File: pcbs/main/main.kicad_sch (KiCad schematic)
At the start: 15 parts

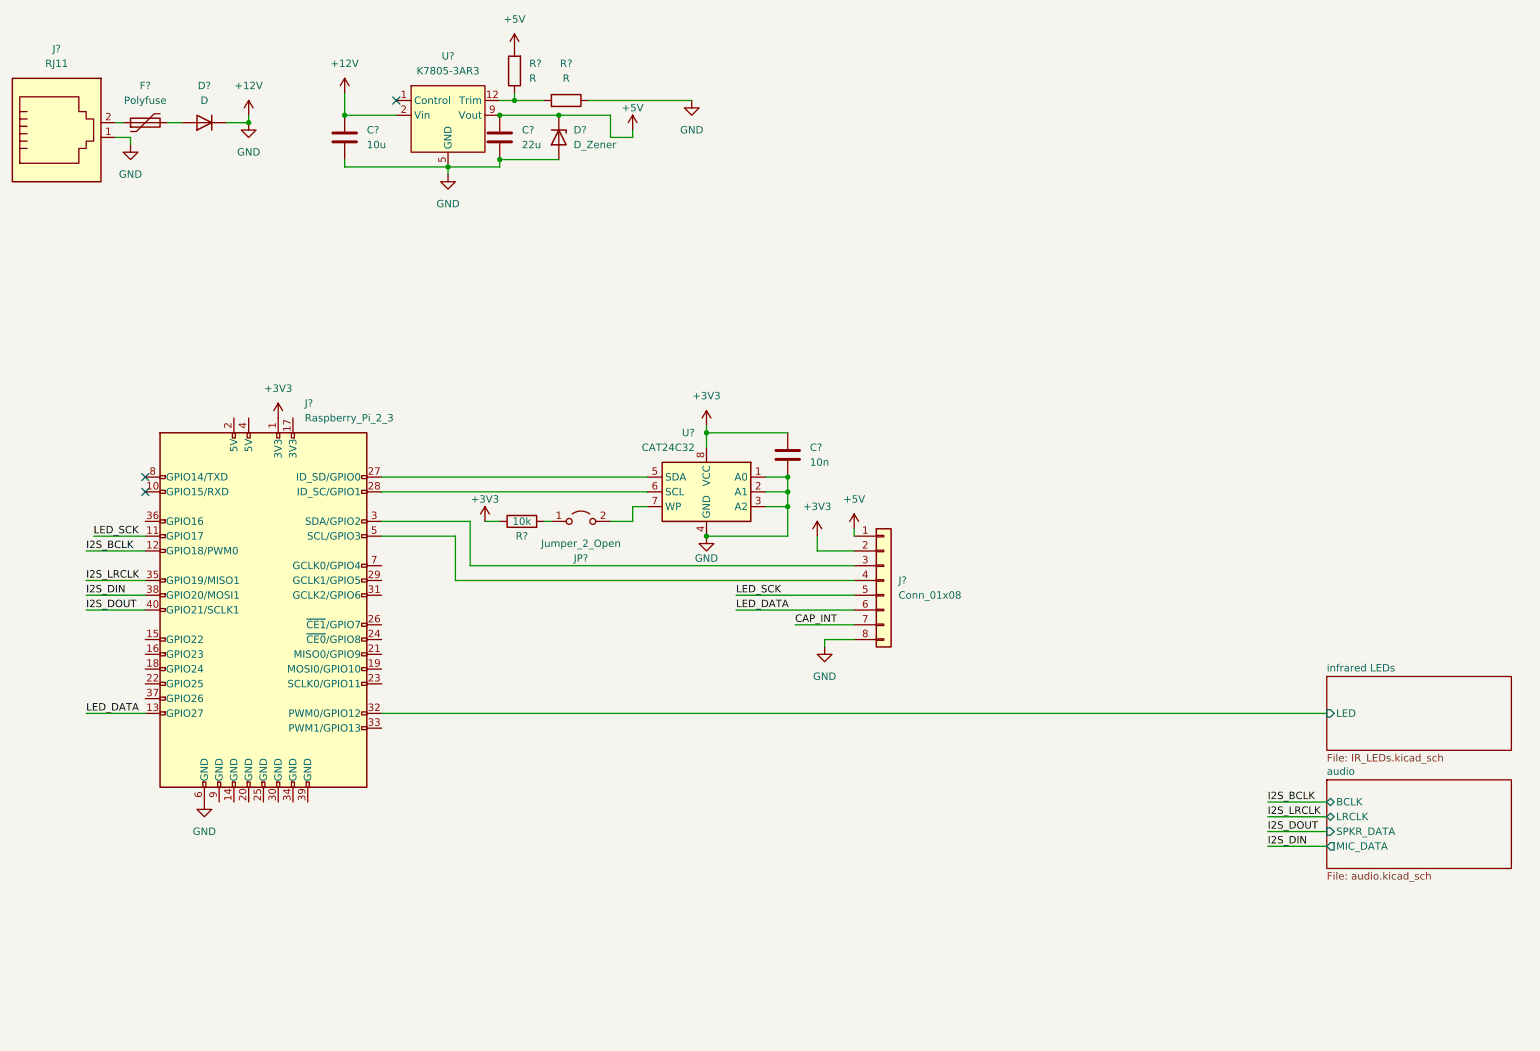
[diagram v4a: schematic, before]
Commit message: Add door release functionality
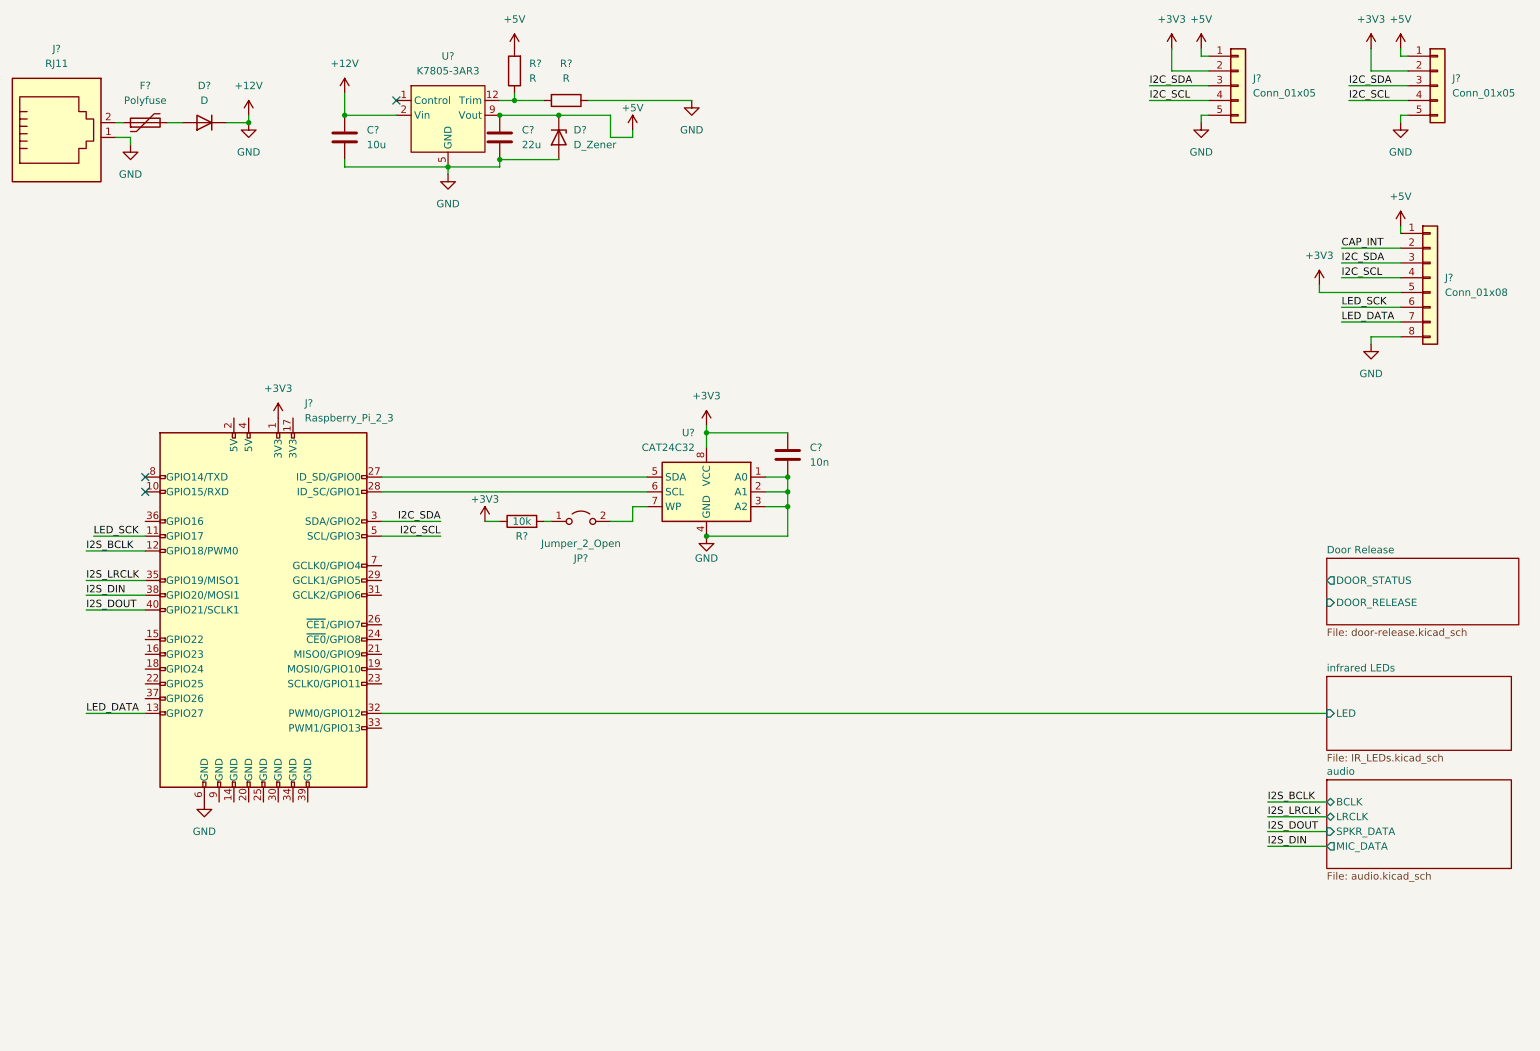
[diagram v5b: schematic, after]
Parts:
- added J? (x2): Conn_01x05, symbol Connector_Generic:Conn_01x05
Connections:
- net +12V: now also J?.5 (Pin_5), J?.5 (Pin_5)
- net +3V3: now also J?.5 (Pin_5), J?.2 (Pin_2), J?.2 (Pin_2); no longer J?.2 (Pin_2)
- net +5V: now also J?.1 (Pin_1), J?.1 (Pin_1)
- net CAP_INT: now also J?.2 (Pin_2); no longer J?.7 (Pin_7)
- net LED_DATA: now also J?.7 (Pin_7); no longer J?.6 (Pin_6)
- net LED_SCK: now also J?.6 (Pin_6); no longer J?.5 (Pin_5)
- net I2C_SDA: now reaches J?.3 (Pin_3), J?.3 (SDA/GPIO2)
- net I2C_SDA: now also J?.3 (Pin_3), J?.3 (Pin_3)
- net I2C_SCL: now reaches J?.4 (Pin_4), J?.5 (SCL/GPIO3)
- net I2C_SCL: now also J?.4 (Pin_4), J?.4 (Pin_4)
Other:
- added sheet Door Release (door-release.kicad_sch)
- moved on the sheet: J?
